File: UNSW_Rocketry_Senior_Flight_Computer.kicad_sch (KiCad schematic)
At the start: 17 parts, among them U1 STM32L452RETx, Y1 8MHz

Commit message: feat: finish schematic (Full)
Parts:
- renumbered C13 to C1, C3 to C10, C1 to C11, C4 to C12, C2 to C13, C12 to C2, C11 to C3, C9 to C4, C8 to C5, C10 to C6, C6 to C7, C7 to C8, C5 to C9

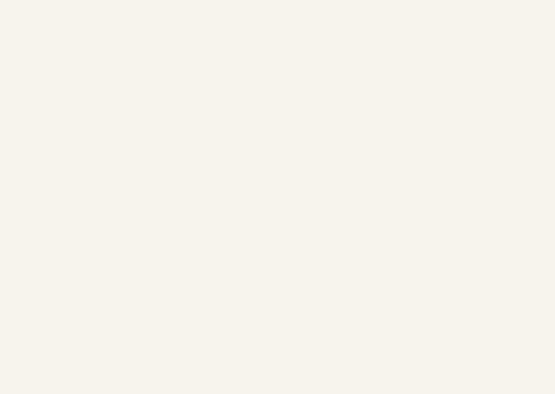
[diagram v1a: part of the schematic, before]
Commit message: feat: BCB Start ( power & pyro done)
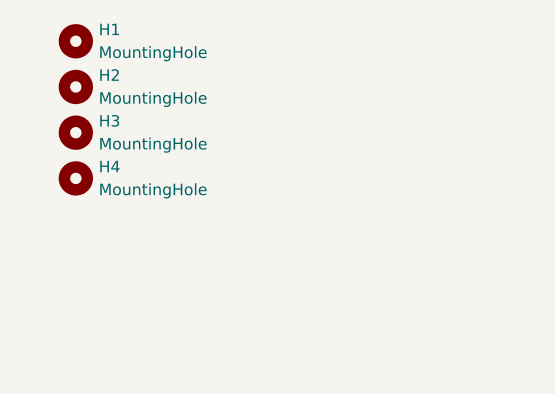
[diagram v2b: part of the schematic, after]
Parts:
- added H1, H2, H3, H4: MountingHole, MountingHole:MountingHole_3.2mm_M3_DIN965_Pad, symbol Mechanical:MountingHole

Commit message: feat: PCB Designed (Silk screen adjustments)
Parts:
- Y1: footprint Crystal:Crystal_SMD_3225-4Pin_3.2x2.5mm_HandSoldering -> Crystal:Crystal_SMD_3225-4Pin_3.2x2.5mm
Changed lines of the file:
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@@
 			)
 		)
-		(property "Footprint" "Crystal:Crystal_SMD_3225-4Pin_3.2x2.5mm_HandSoldering"
+		(property "Footprint" "Crystal:Crystal_SMD_3225-4Pin_3.2x2.5mm"
 			(at 170.18 43.18 0)
 			(hide yes)
